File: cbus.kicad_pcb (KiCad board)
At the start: 2 copper layers, 50 x 150 mm, 32 parts, among them CON1 AVR-JTAG-10, J1 CBUS_IO, J2 Conn_02x20_Odd_Even, J3 Conn_02x05_Top_Bottom, J4 Conn_02x05_Top_Bottom, U1 SN74LVC8T245DWR, U2 SN74LVC8T245DWR, U3 SN74LVC8T245DWR, U4 SN74LVC8T245DWR, U5 MIC5365-1.2YC5-TR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

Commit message: Finish routing
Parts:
- added ?: MountingHole_3.2mm_M3, Mounting_Holes:MountingHole_3.2mm_M3, F.Cu at (75.0, 172.0)
- added ?: MountingHole_3.2mm_M3, Mounting_Holes:MountingHole_3.2mm_M3, F.Cu at (75.0, 30.0)
- added R3: 1, Resistors_SMD:R_0805_HandSoldering, F.Cu at (48.5, 45.2)
- added R4: 1, Resistors_SMD:R_0805_HandSoldering, F.Cu at (48.5, 53.2)
- C2, C3: value 1uF -> 4.7uF
- U5: value MIC5365-1.2YC5-TR -> TPS76933; footprint tinyfpga:SC-70-C5 -> TO_SOT_Packages_SMD:SOT-23-5
- U7: value MIC5504-3.3YM5-TR -> TPS76912; footprint tinyfpga:SC-70-C5 -> TO_SOT_Packages_SMD:SOT-23-5
- moved U7 19.7 mm to (46.3, 49.6)
- moved C3 19.2 mm to (51.5, 50.0), turned to 270 degrees
- moved U5 9.04 mm to (46.8, 41.2)
- moved C2 7.69 mm to (51.4, 41.4), turned to 270 degrees
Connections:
- C2 pad 2: GND -> Net-(C2-Pad2)
- C3 pad 2: GND -> Net-(C3-Pad2)
- U5 pad 1: +3V3 -> +5V
- U5 pad 3: +3V3 -> GND
- U5 pad 4: +1V2 -> Net-(U5-Pad4)
- U5 pad 5: +1V2 -> +3V3
- U6 pad 17: Net-(U6-Pad17) -> GND
- U6 pad 23: Net-(U6-Pad17) -> GND
- U6 pad 32: Net-(U6-Pad17) -> GND
- U6 pad 39: Net-(U6-Pad17) -> GND
- U6 pad 47: Net-(U6-Pad17) -> GND
- U6 pad 5: Net-(U6-Pad17) -> GND
- U6 pad 55: Net-(U6-Pad17) -> GND
- U6 pad 70: Net-(U6-Pad17) -> GND
- U6 pad 84: Net-(U6-Pad17) -> GND
- U6 pad 98: Net-(U6-Pad17) -> GND
- U7 pad 1: +5V -> +3V3
- U7 pad 3: +5V -> GND
- U7 pad 4: +3V3 -> Net-(U7-Pad4)
- U7 pad 5: +3V3 -> +1V2
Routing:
- net GND: track 0.00 -> 200.2 mm, vias 0 -> 38
- net +5V: track 11.7 -> 172.0 mm, vias 0 -> 6
- net +1V2: track 33.9 -> 128.8 mm
- net RESET: track 12.8 -> 87.8 mm, vias 0 -> 1
- net Net-(J1-PadB8): track 0.00 -> 68.4 mm
- net +3V3: track 10.8 -> 71.6 mm, vias 0 -> 10
- net A04_33: track 59.1 -> 24.5 mm
- net Net-(J1-PadA46): track 0.00 -> 18.4 mm, vias 0 -> 1
- net A10_33: track 46.5 -> 64.0 mm
- net DIR: track 16.8 -> 24.0 mm
- net A15_33: track 44.2 -> 50.4 mm
- net Net-(J1-PadB4): track 73.9 -> 77.3 mm
- net Net-(C2-Pad2): track 0.00 -> 3.26 mm
- net Net-(C3-Pad2): track 0.00 -> 2.71 mm
- net D0: track 99.6 -> 97.3 mm
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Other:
- net class Default: clearance 0.2 -> 0.16; trace_width 0.25 -> 0.2; via_drill 0.4 -> 0.3
- net class Ground added: clearance 0.16, trace_width 0.5, via_dia 0.6, via_drill 0.3
- rule trace_clearance: 0.2 -> 0.16
- rule trace_min: 0.2 -> 0.1524
- rule via_min_drill: 0.3 -> 0.254
- rule via_min_size: 0.4 -> 0.508

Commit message: 1.0
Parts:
- added REF**: KiCAD Logo, Symbols:Symbol_KiCAD-Logo_CopperAndSilkScreenTop, F.Cu at (49.7, 170.3)
- added REF***: OSHW-Logo_7.5x8mm_SilkScreen, Symbols:OSHW-Logo_7.5x8mm_SilkScreen, F.Cu at (62.9, 170.1)
- added svg2mod: G***, cbus:alice2, F.Cu at (74.5, 42.5)
- U1, U2, U3, U4: footprint SN74LVC8T245DWR:SOIC127P1030X265-24N -> cbus:SOIC127P1030X265-24N
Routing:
- net +3V3: track 71.6 -> 77.2 mm, vias 10 -> 11
- net D0: track 97.3 -> 97.8 mm
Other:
- board size 50 x 150 mm -> 50 x 149 mm
- board text added: "PC-98 Joystick Interface 1.0 CC-BY 2018 TD-Linux"

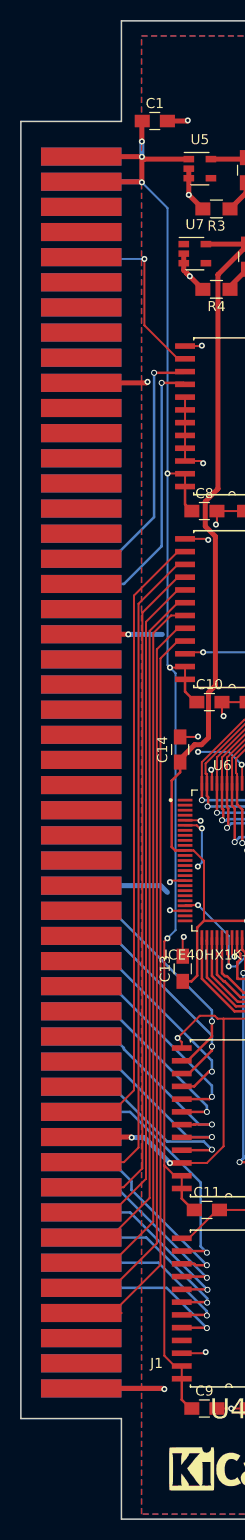
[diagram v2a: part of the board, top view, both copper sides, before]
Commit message: Fix connector spacing
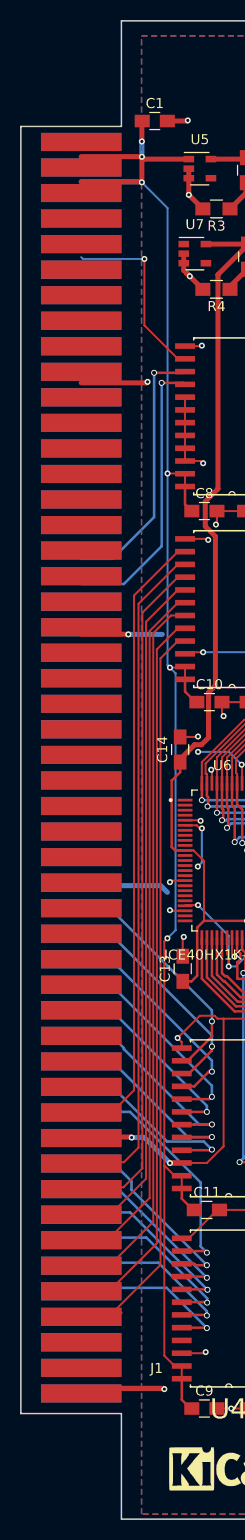
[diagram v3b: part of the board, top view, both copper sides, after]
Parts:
- moved J1 0.50 mm to (35.0, 163.0)
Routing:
- net GND: track 200.1 -> 185.3 mm, vias 38 -> 36
- net (no net): track 0.00 -> 14.7 mm, vias 0 -> 2
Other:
- outline, holes or cut-outs redrawn

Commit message: Longboi
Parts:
- J3, J4: value Conn_02x05_Top_Bottom -> DB9_Male; footprint cbus:Pin_Header_Straight_2x05_Pitch2.54mm_Column_first -> Connector_Dsub:DSUB-9_Male_Horizontal_P2.77x2.84mm_EdgePinOffset4.94mm_Housed_MountingHolesOffset7.48mm
- moved svg2mod 140.1 mm to (204.0, 96.0)
- moved J4 131.3 mm to (201.0, 127.0), turned to 90 degrees
- moved J3 127.8 mm to (201.0, 77.0), turned to 90 degrees
- moved ? 127.1 mm to (202.0, 166.0)
- moved ? 126.1 mm to (201.0, 34.0)
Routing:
- net SDO: track 100.2 -> 53.2 mm, vias 5 -> 2
- net P2B: track 44.4 -> 0.00 mm, vias 1 -> 0
- net P2U: track 42.9 -> 0.00 mm, vias 1 -> 0
- net P2D: track 41.8 -> 0.00 mm, vias 1 -> 0
- net P2S: track 40.8 -> 0.00 mm, vias 1 -> 0
- net P2L: track 37.4 -> 0.00 mm, vias 2 -> 0
- net P2C: track 33.1 -> 0.00 mm, vias 2 -> 0
- net P2R: track 32.5 -> 0.00 mm, vias 4 -> 0
- net P1B: track 29.9 -> 0.00 mm
- net P1S: track 29.5 -> 0.00 mm
- net P1U: track 28.6 -> 0.00 mm
- net P1D: track 27.9 -> 0.00 mm
- net P1C: track 27.0 -> 0.00 mm
- net P1L: track 25.4 -> 0.00 mm
- net P1R: track 24.2 -> 0.00 mm
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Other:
- board size 50 x 149 mm -> 180 x 149 mm
- board text added: "PC-98 Joystick Interface 1.1 CC-BY 2018 TD-Linux"
- board text removed: "PC-98 Joystick Interface 1.0 CC-BY 2018 TD-Linux"
